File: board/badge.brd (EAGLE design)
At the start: 157.3 x 91.3 mm, 43 parts, among them J1 SWD_PTH_SHROUD, X1 SMA-142-0701-851/861, X2 1503_02

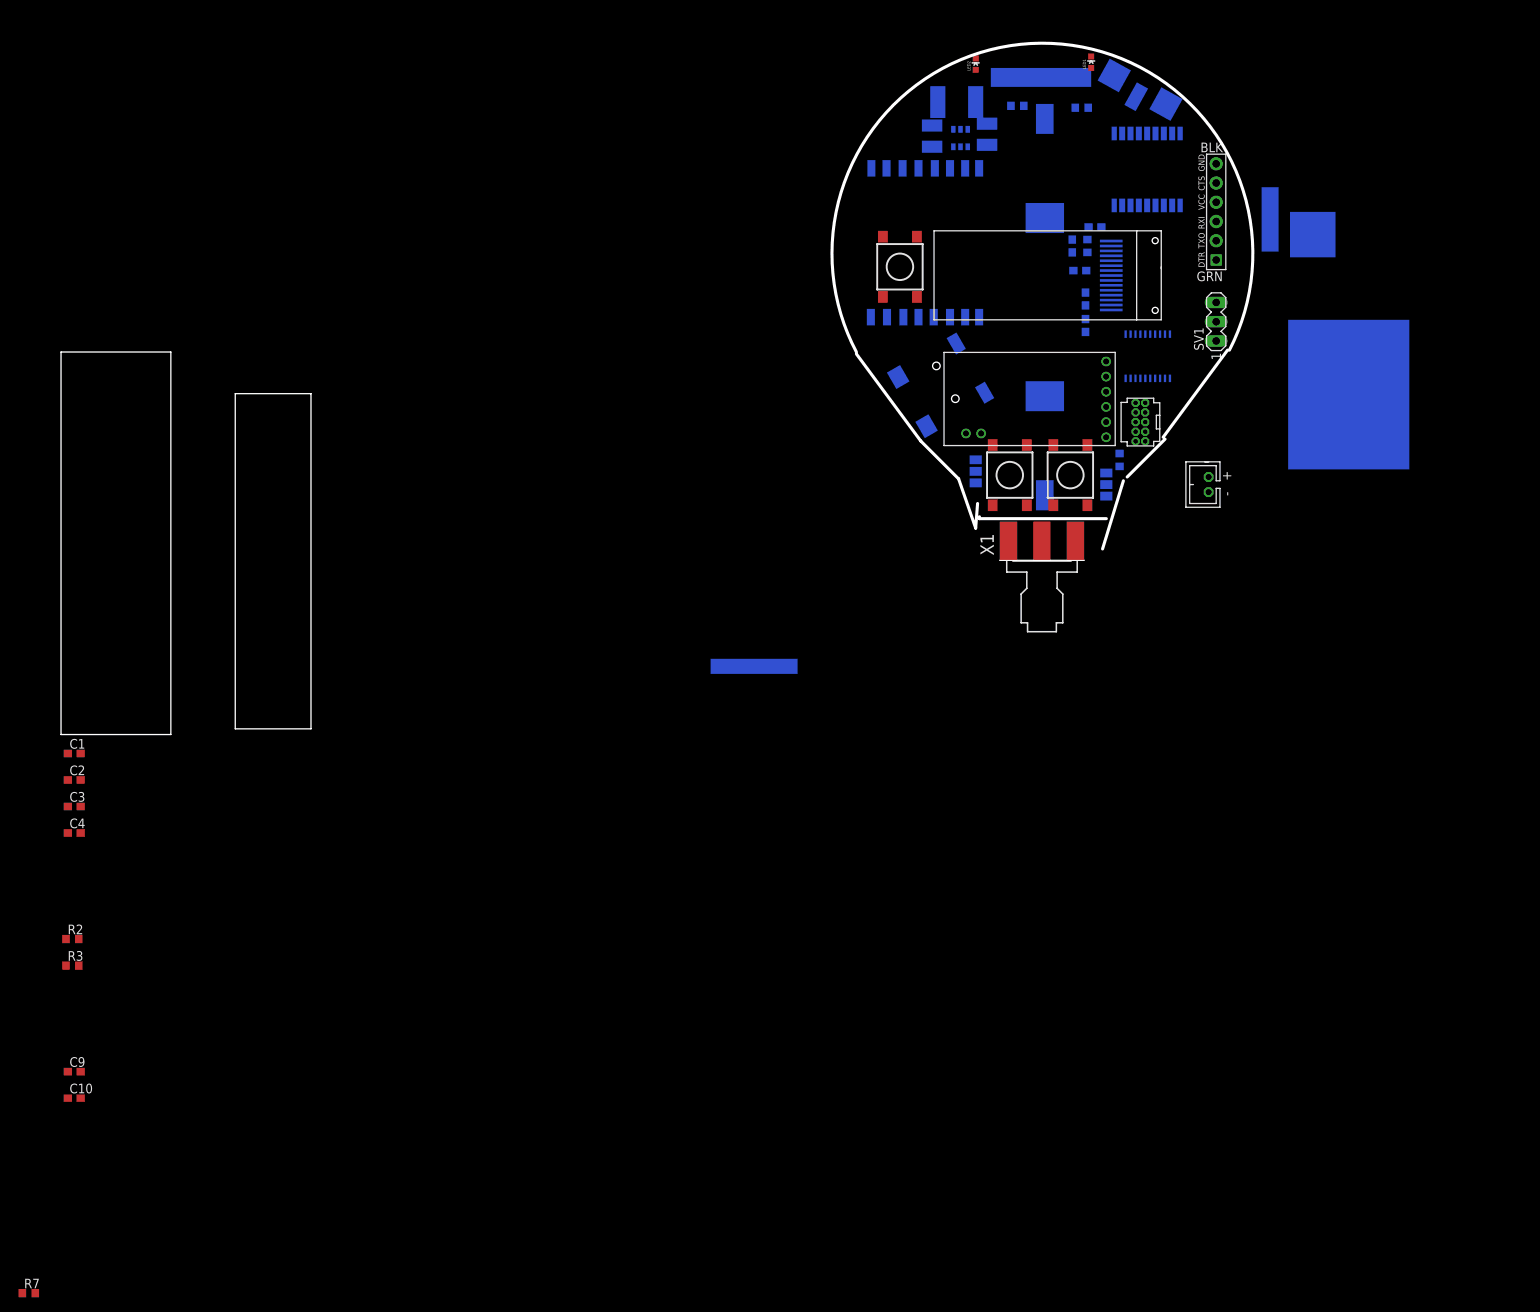
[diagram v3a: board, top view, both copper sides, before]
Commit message: initial route
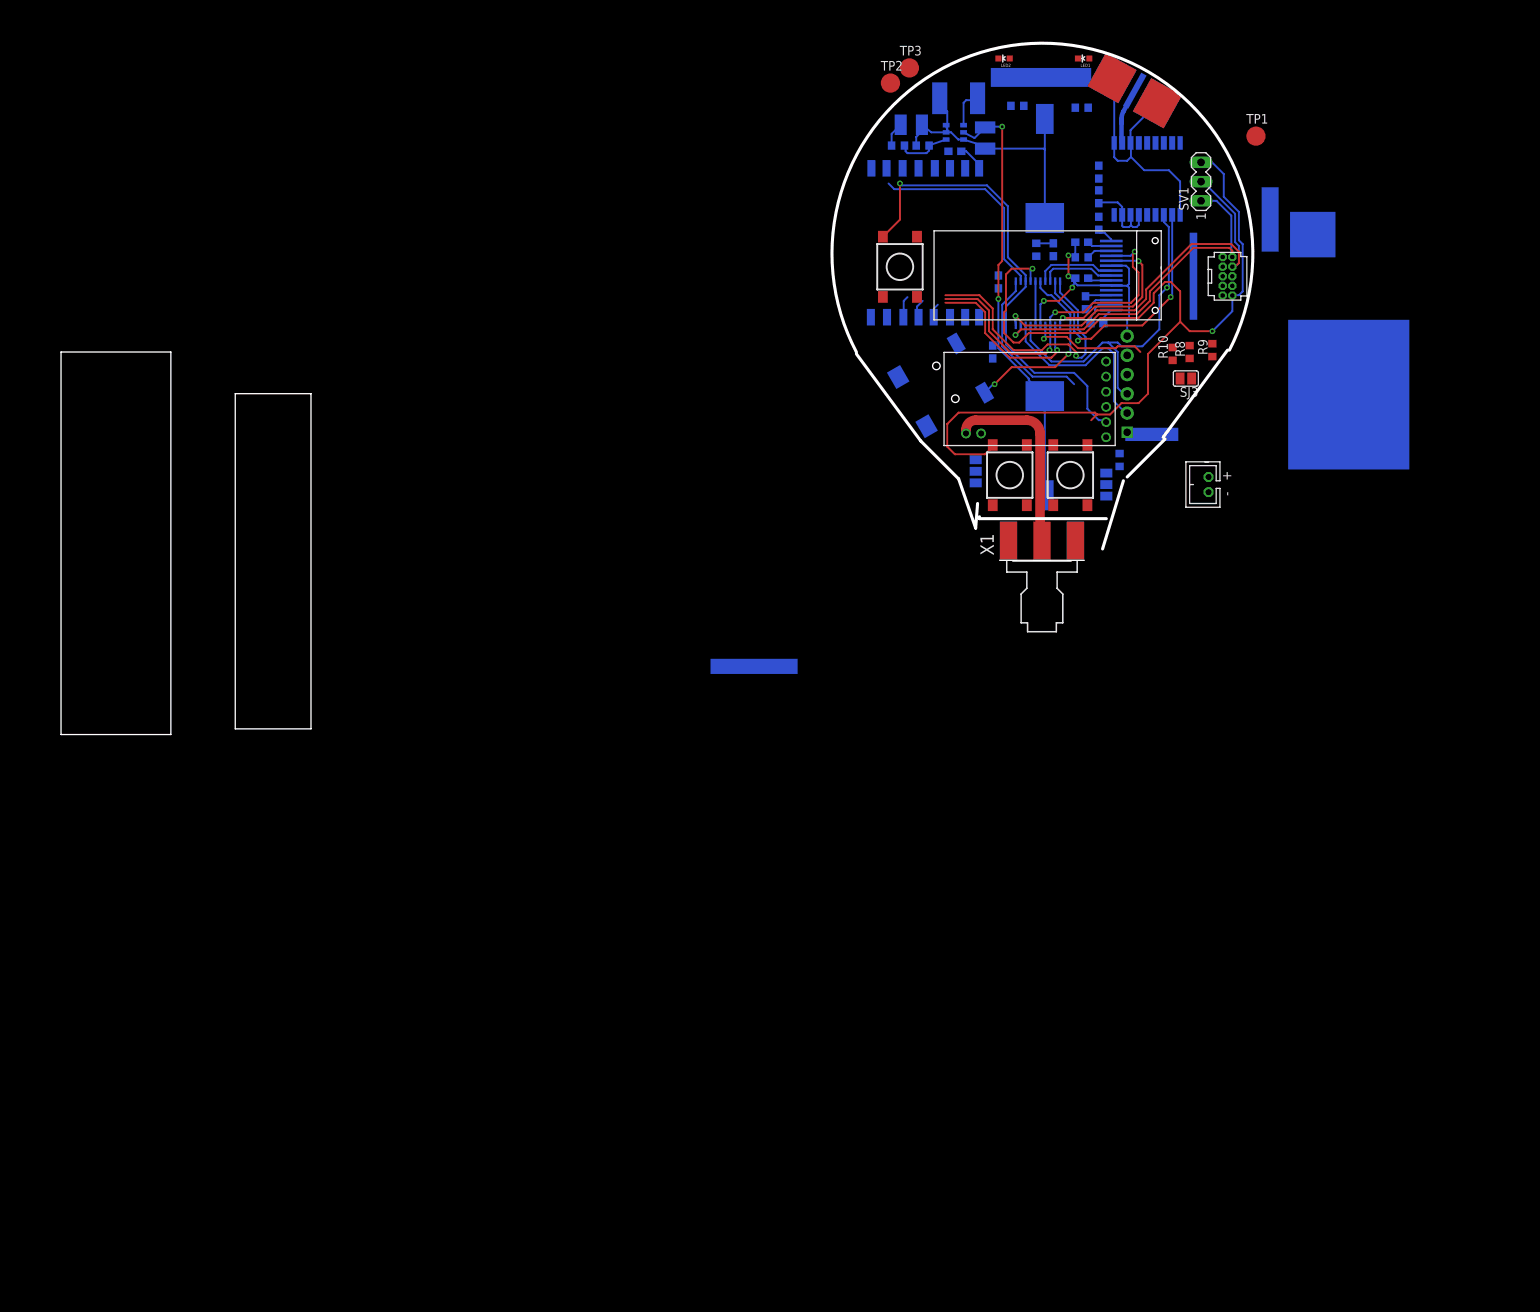
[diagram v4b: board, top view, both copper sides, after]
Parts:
- removed U$11: MCP1640, ukhas:SOT23-6
- removed U$2: STM32F030F4, dtb:TSSOP20
- removed U$3: UBLOX_MAX, Ava:UBLOX_MAX
- removed U$9: SARANTEL-SL1250, Ava:SARANTEL-SL1250
- added IC1: STM32F030F4, dtb:TSSOP20
- added IC2: UBLOX_MAX, Ava:UBLOX_MAX
- added IC3: MCP1640, ukhas:SOT23-6
- added R10, R8, R9: (no value), rcl:R0603
- added SJ3: (no value), jumper:SJ
- added TP1, TP2, TP3: PTR1B2,54, testpad:B2,54
- added U$5: JDGA-REMQV-ANTENNA, Ava:JDGA-RIGID_COMBO_PAD
- moved R7 191.5 mm to (31.5, 54.0), flipped to the bottom, turned to 90 degrees
- moved C9 168.2 mm to (20.8, 67.0), flipped to the bottom
- moved C4 159.2 mm to (39.8, 61.0), flipped to the bottom, turned to 90 degrees
- moved C3 159.1 mm to (39.8, 64.2), flipped to the bottom, turned to 90 degrees
- moved C10 156.2 mm to (25.8, 40.5), flipped to the bottom, turned to 270 degrees
- moved R3 153.6 mm to (13.2, 67.8), flipped to the bottom, turned to 180 degrees
- moved R2 153.5 mm to (16.5, 67.8), flipped to the bottom
- moved C1 145.4 mm to (33.8, 54.0), flipped to the bottom, turned to 90 degrees
- moved C2 138.6 mm to (26.5, 49.8), flipped to the bottom, turned to 90 degrees
- moved JP1 25.6 mm to (43.5, 36.2), flipped to the bottom
- moved J1 22.4 mm to (56.8, 50.5), turned to 270 degrees
- moved SV1 18.6 mm to (53.2, 63.0)
- moved LED2 3.82 mm to (27.2, 79.2), turned to 90 degrees
- moved C8 3.13 mm to (15.0, 70.5), turned to 0 degrees
- moved R4 1.68 mm to (37.5, 53.0), turned to 180 degrees
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- renumbered U$1 to X3, U$10 to IC4, U$8 to X4
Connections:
- new net N$21: R8.2, SJ3.1, X4.TXD
- net +3V3: now also IC1.16, IC1.5, IC2.6_V_BCKP, IC2.7_VCC_IO, IC2.8_VCC, IC3.5, JP1.P$4, R9.1, TP1.TP; no longer U$11.5, U$2.16, U$2.5, U$3.6_V_BCKP, U$3.7_VCC_IO, U$3.8_VCC
- net 0V: now also IC1.15, IC2.10_GND, IC2.12_GND, IC2.1_GND, IC3.2, R10.2, TP2.TP, U$5.P$2, U$5.P$3, U$5.P$4, U$5.P$5; no longer U$11.2, U$2.15, U$3.10_GND, U$3.12_GND, U$3.1_GND, U$9.P$1, U$9.P$3
- net 9_V_RESET: now also IC2.9_V_RESET; no longer U$3.9_V_RESET
- net ADC1: now also IC1.6; no longer U$2.6
- net CS: now also IC1.10; no longer U$2.10
- net DIO0: now also IC1.2; no longer U$2.2
- net MISO: now also IC1.12; no longer U$2.12
- net MOSI: now also IC1.13; no longer U$2.13
- net N$1: now also IC2.11_RF_IN, U$5.P$1; no longer U$3.11_RF_IN, U$9.P$2
- net N$14: now also IC3.4; no longer U$11.4
- net N$15: now also IC3.1; no longer U$11.1
- net N$2: now also IC1.9, IC2.2_TXD1, TP3.TP; no longer U$2.9, U$3.2_TXD1
- net N$7: now also IC1.1; no longer U$2.1
- net N$8: now also IC1.17, IC2.3_RXD1; no longer U$2.17, U$3.3_RXD1
- net N$9: now also IC1.18; no longer U$2.18
- net NRST: now also IC1.4; no longer U$2.4
- net O_CS: now also IC1.8; no longer U$2.8
- net O_RES: now also IC1.7; no longer U$2.7
- net SCK: now also IC1.11; no longer U$2.11
- net SWCLK: now also IC1.20; no longer U$2.20
- net SWDAT: now also IC1.19; no longer U$2.19
- net TX: now also IC1.14, R10.1, R8.1, R9.2, SJ3.2; no longer U$2.14, X4.TXD
- net TX_EN: now also IC1.3; no longer U$2.3
- net VIN: now also IC3.3, IC3.6; no longer U$11.3, U$11.6
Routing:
- net 0V: track 0.00 -> 131.7 mm, vias 0 -> 6
- net NRST: track 0.00 -> 128.8 mm, vias 0 -> 2
- net TX_EN: track 0.00 -> 63.0 mm, vias 0 -> 1
- net SWCLK: track 0.00 -> 53.4 mm, vias 0 -> 1
- net MOSI: track 0.00 -> 48.5 mm, vias 0 -> 3
- net SWDAT: track 0.00 -> 47.0 mm, vias 0 -> 1
- net N$8: track 0.00 -> 46.6 mm, vias 0 -> 1
- net CS: track 0.00 -> 35.6 mm, vias 0 -> 1
- net N$2: track 0.00 -> 35.2 mm, vias 0 -> 2
- net VIN: track 0.00 -> 32.8 mm
- net +3V3: track 0.00 -> 31.0 mm
- net DIO0: track 0.00 -> 27.1 mm
- net MISO: track 0.00 -> 25.8 mm, vias 0 -> 1
- net N$4: track 0.00 -> 25.8 mm
- net N$9: track 0.00 -> 25.0 mm
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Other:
- board text added: "3.3V only"
- board text added: "Remove battery"
- board text added: "see how far led cable comes out"

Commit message: routing almost done
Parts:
- removed R10, R8, R9: (no value), rcl:R0603
- removed SJ3: (no value), jumper:SJ
- added TP4: PTR1B2,54, testpad:B2,54
- SV1: device con-lstb:MA03-1 -> Mine:MA03-1
- moved TP3 49.7 mm to (49.5, 42.5), flipped to the bottom
- moved C10 45.1 mm to (57.0, 73.0)
- moved TP1 29.9 mm to (30.8, 71.8)
- moved R1 29.5 mm to (28.5, 52.2), turned to 180 degrees
- moved TP2 23.6 mm to (35.5, 71.8)
- moved C2 6.95 mm to (32.0, 54.0)
- moved R7 3.01 mm to (28.5, 54.2), turned to 180 degrees
- moved R5 1.68 mm to (39.0, 72.0), turned to 180 degrees
- moved SJ1 1.50 mm to (40.8, 24.5)
- moved U$5 1.27 mm to (45.8, 74.8), turned to 32 degrees
- moved IC4 1.03 mm to (26.0, 64.5)
- moved SV1 0.75 mm to (53.2, 62.2), flipped to the bottom, turned to 270 degrees
- moved C12 0.50 mm to (38.0, 55.0)
- moved R4 0.50 mm to (38.0, 53.0)
- moved C1 0.25 mm to (34.0, 54.0)
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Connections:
- removed net N$21: R8.2, SJ3.1, X4.TXD
- net +3V3: no longer R9.1
- net 0V: no longer R10.2
- net N$6: now also TP4.TP
- net TX: now also X4.TXD; no longer R10.1, R8.1, R9.2, SJ3.2
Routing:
- net 0V: track 131.7 -> 380.8 mm, vias 6 -> 17
- net +3V3: track 31.0 -> 207.0 mm, vias 0 -> 10
- net N$6: track 0.00 -> 83.8 mm, vias 0 -> 1
- net N$18: track 0.00 -> 33.0 mm, vias 0 -> 1
- net NRST: track 128.8 -> 97.8 mm, vias 2 -> 3
- net N$20: track 0.00 -> 18.8 mm
- net SCK: track 23.2 -> 41.2 mm, vias 2 -> 3
- net SWDAT: track 47.0 -> 64.3 mm, vias 1 -> 2
- net N$19: track 0.00 -> 13.4 mm, vias 0 -> 1
- net N$7: track 20.9 -> 33.2 mm, vias 0 -> 1
- net CS: track 35.6 -> 46.7 mm, vias 1 -> 2
- net TX: track 15.7 -> 25.4 mm
- net SWCLK: track 53.4 -> 61.9 mm, vias 1 -> 3
- net MOSI: track 48.5 -> 55.1 mm, vias 3 -> 4
- net N$2: track 35.2 -> 41.5 mm
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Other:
- outline, holes or cut-outs redrawn
- board text added: "BOOT"
- board text added: "CLK"
- board text added: "DIO"
- board text added: "RESET"
- board text added: "RST"
- board text added: "SWD"
- board text removed: "see how far led cable comes out"

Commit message: almost done
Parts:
- removed C13: 1u, rcl:C0603
- removed TP4: PTR1B2,54, testpad:B2,54
- removed U$4: INDUCTOR, ukhas:INDUCTOR5X5
- removed U$6: (no value), ukhas:0.91OLEDPANEL
- removed X4: RADIOMETRIX-MTX2, Ava:RADIOMETRIX-MTX2
- added L1: INDUCTOR, ukhas:INDUCTOR5X5
- added U$1: (no value), ukhas:0.91OLEDPANEL
- C1, C2, C4: value (none) -> 1u
- C11, C12: value 2u2 -> (none); device rcl:C0603 -> rcl:C0805
- C5, C6: value 1u -> (none)
- C7, C8: value (none) -> 2u2; device rcl:C1210 -> rcl:C0603
- IC3: value MCP1640 -> RFM69HW; device ukhas:SOT23-6 -> hoperf:RFM
- IC4: value RFM69HW -> MCP1640; device hoperf:RFM -> ukhas:SOT23-6
- J2: value (none) -> 20-0096; device dtb:JST-2-TH -> ukhas:3.5MMLOWPROFILE
- R3: value (none) -> 1k
- R7: value 1k -> (none)
- X1: value SMA-142-0701-851/861 -> RADIOMETRIX-MTX2; device con-coax:J502-ND-142-0701-851/861 -> Ava:RADIOMETRIX-MTX2
- X2: value 1503_02 -> SMA-142-0701-851/861; device con-lumberg:1503_02 -> con-coax:J502-ND-142-0701-851/861
- moved J2 44.6 mm to (12.0, 37.2), flipped to the bottom, turned to 153 degrees
- moved S3 36.0 mm to (36.8, 24.2)
- moved S1 30.2 mm to (15.0, 51.5)
- moved C8 28.0 mm to (39.8, 57.5), turned to 270 degrees
- moved X2 27.1 mm to (32.6, 13.8), flipped to the top, turned to 90 degrees
- moved R2 25.9 mm to (38.0, 53.2), turned to 180 degrees
- moved C12 24.6 mm to (18.0, 69.2)
- moved R5 23.7 mm to (15.8, 67.2)
- moved R4 23.6 mm to (19.2, 67.2), turned to 0 degrees
- moved X1 22.8 mm to (30.8, 35.8), turned to 0 degrees
- moved R3 20.4 mm to (28.5, 54.2)
- moved C9 19.9 mm to (39.8, 61.0), turned to 90 degrees
- moved C10 19.3 mm to (39.8, 64.2), turned to 90 degrees
- moved C7 19.3 mm to (38.0, 55.0), turned to 0 degrees
- moved R7 19.3 mm to (36.0, 72.0), turned to 0 degrees
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- renumbered B2 to B1, J1 to J3, U$5 to U$2
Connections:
- net +3V3: now also C12.1, C4.2, C5.1, C6.1, IC3.VCC, IC4.5, LED2.A, R4.2, S3.A2, X1.VCC; no longer C1.1, C13.2, C2.1, C4.1, C8.1, IC3.5, IC4.VCC, LED1.A, R2.2, S2.A2, X4.VCC
- net 0V: now also C11.2, C4.1, C5.2, C6.2, C8.1, IC3.GNDA, IC3.GNDB, IC4.2, J2.2_1, J2.2_2, LED1.C, R2.1, R3.2, R5.1, S2.A2, X1.GND, X1.RFGND, X2.G@1, X2.G@2, X2.G@3, X2.G@4; no longer C1.2, C11.1, C13.1, C2.2, C4.2, C8.2, IC3.2, IC4.GNDA, IC4.GNDB, LED2.C, R3.1, R4.1, R7.2, S1.A2, X1.G@1, X1.G@2, X1.G@3, X1.G@4, X2.2, X4.GND, X4.RFGND
- net ADC1: now also J2.4_1, J2.4_2; no longer X2.3
- net CS: now also IC3.NSS; no longer IC4.NSS
- net DIO0: now also IC3.DIO0; no longer IC4.DIO0
- net MISO: now also IC3.MISO; no longer IC4.MISO
- net MOSI: now also IC3.MOSI; no longer IC4.MOSI
- net N$10: now also C2.2; no longer C5.2
- net N$11: now also C1.2; no longer C6.2
- net N$12: now also C2.1; no longer C5.1
- net N$13: now also C1.1; no longer C6.1
- net N$14: now also IC4.4, R4.1, R5.2; no longer IC3.4, R2.1, R3.2
- net N$15: now also IC4.1, L1.P$2; no longer IC3.1, U$4.P$2
- net N$16: now also C7.1; no longer C12.1
- net N$17: now also LED1.A, R7.1; no longer LED2.A, R6.1
- net N$18: now also X1.P1; no longer X4.P1
- net N$19: now also R3.1, S1.A2; no longer R7.1, S3.A2
- net N$20: now also X1.P0; no longer X4.P0
- net N$3: now also LED2.C, R6.2; no longer LED1.C, R5.2
- net N$4: now also X1.RF, X2.1; no longer X1.1, X4.RF
- net N$5: now also R2.2; no longer R4.2
- net N$6: now also IC3.ANT; no longer IC4.ANT, TP4.TP
- net N$7: now also S3.B2; no longer S2.B2
- net NRST: now also S2.B2; no longer S1.B2
- net SCK: now also IC3.SCK; no longer IC4.SCK
- net SWCLK: now also R7.2; no longer R6.2
- net SWDAT: now also R6.1; no longer R5.1
- net TX: now also X1.TXD; no longer X4.TXD
- net TX_EN: now also S1.B2, X1.EN; no longer S3.B2, X4.EN
- net VCC: now also C8.2; no longer C11.2
- net VIN: now also C11.1, IC4.3, IC4.6, L1.P$1; no longer C7.1, IC3.3, IC3.6, U$4.P$1
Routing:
- net 0V: track 380.8 -> 318.4 mm, vias 17 -> 114
- net SWCLK: track 61.9 -> 98.9 mm, vias 3 -> 4
- net SWDAT: track 64.3 -> 101.0 mm, vias 2 -> 3
- net N$17: track 0.00 -> 13.0 mm, vias 0 -> 1
- net N$18: track 33.0 -> 36.6 mm
- net N$3: track 0.00 -> 3.54 mm, vias 0 -> 1
- net N$6: track 83.8 -> 81.3 mm
- net ADC1: track 24.8 -> 27.2 mm
- net +3V3: track 207.0 -> 209.0 mm, vias 10 -> 9
- net N$20: track 18.8 -> 16.8 mm
- net N$9: track 25.0 -> 23.1 mm
- net NRST: track 97.8 -> 96.2 mm
- net N$4: track 25.8 -> 26.7 mm
- net MOSI: track 55.1 -> 54.3 mm
- net N$14: track 7.21 -> 6.39 mm
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- added copper zone on layer 1, net 0V
- added copper zone on layer 16, net 0V
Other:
- board size 157.3 x 91.3 mm -> 157.7 x 91.3 mm
- board text added: "0"
- board text added: "1"
- board text added: "3.3V"
- board text added: "GND"
- board text added: "GPS TX"
- board text added: "P0"
- board text added: "P1"
- board text added: "Rev. A May '14"
